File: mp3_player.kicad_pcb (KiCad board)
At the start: 4 copper layers, 0 parts

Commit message: PCB: outline, port cutouts, ESP32 placement
- board outline from pcb_outline_B.dxf, centred on the page, drill/place
  and grid origin at the bottom-left corner (130, 155)
- USB-C and jack cutouts drawn on the board outline instead of the
  footprints; jack pads trimmed for 0.2 mm to the slot, custom DRC rule
  allows 0.2 mm edge clearance for those pads only
- ESP32 on the centre line with the antenna at the top edge, antenna
  keepout on all copper layers
- microSD peg holes made non-plated

Co-Authored-By: Claude Opus 5.5 <noreply@anthropic.com>
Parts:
- added BT1: Battery_Cell, mp3_player:CONN-SMD_2P-P1.00_SM02B-SRSS-TB-LF-SN, F.Cu at (210.1, 74.1)
- added C1: C, Capacitor_SMD:C_0402_1005Metric, F.Cu at (208.7, 62.0)
- added C10: C, Capacitor_SMD:C_0603_1608Metric, F.Cu at (207.7, 100.3)
- added C11: C, Capacitor_SMD:C_0402_1005Metric, F.Cu at (208.7, 69.9)
- added C12: C, Capacitor_SMD:C_0603_1608Metric, F.Cu at (207.7, 102.9)
- added C13: C, Capacitor_SMD:C_0603_1608Metric, F.Cu at (211.7, 92.8)
- added C14: C, Capacitor_SMD:C_0603_1608Metric, F.Cu at (211.7, 95.3)
- added C15: C, Capacitor_SMD:C_0603_1608Metric, F.Cu at (211.7, 97.8)
- added C16: C, Capacitor_SMD:C_0402_1005Metric, F.Cu at (211.5, 62.0)
- added C17: C, Capacitor_SMD:C_0805_2012Metric, F.Cu at (225.4, 85.2)
- added C18: C, Capacitor_SMD:C_0402_1005Metric, F.Cu at (211.5, 64.0)
- added C19: C, Capacitor_SMD:C_0603_1608Metric, F.Cu at (211.7, 100.3)
- added C2: C, Capacitor_SMD:C_0603_1608Metric, F.Cu at (207.7, 92.8)
- added C20: C, Capacitor_SMD:C_0402_1005Metric, F.Cu at (211.5, 65.9)
- added C21: C, Capacitor_SMD:C_0603_1608Metric, F.Cu at (211.7, 102.9)
- added C22: C, Capacitor_SMD:C_0402_1005Metric, F.Cu at (211.5, 67.9)
- added C23: C, Capacitor_SMD:C_0805_2012Metric, F.Cu at (225.4, 88.2)
- added C24: C, Capacitor_SMD:C_0402_1005Metric, F.Cu at (211.5, 69.9)
- added C25: C, Capacitor_SMD:C_0402_1005Metric, F.Cu at (214.4, 62.0)
- added C26: C, Capacitor_SMD:C_0402_1005Metric, F.Cu at (214.4, 64.0)
- added C27: C, Capacitor_SMD:C_0603_1608Metric, F.Cu at (215.7, 92.8)
- added C28: C, Capacitor_SMD:C_0402_1005Metric, F.Cu at (214.4, 65.9)
- added C29: C, Capacitor_SMD:C_0603_1608Metric, F.Cu at (215.7, 95.3)
- added C3: C, Capacitor_SMD:C_0402_1005Metric, F.Cu at (208.7, 64.0)
- added C30: C, Capacitor_SMD:C_0402_1005Metric, F.Cu at (214.4, 67.9)
- added C31: C, Capacitor_SMD:C_0603_1608Metric, F.Cu at (215.7, 97.8)
- added C32: C, Capacitor_SMD:C_0603_1608Metric, F.Cu at (215.7, 100.3)
- added C33: C, Capacitor_SMD:C_0402_1005Metric, F.Cu at (214.4, 69.9)
- added C34: C, Capacitor_SMD:C_0603_1608Metric, F.Cu at (215.7, 102.9)
- added C35: C, Capacitor_SMD:C_0402_1005Metric, F.Cu at (217.3, 62.0)
- added C36: C, Capacitor_SMD:C_0603_1608Metric, F.Cu at (219.7, 92.8)
- added C37: C, Capacitor_SMD:C_0402_1005Metric, F.Cu at (217.3, 64.0)
- added C38: C, Capacitor_SMD:C_0603_1608Metric, F.Cu at (219.7, 95.3)
- added C39: C, Capacitor_SMD:C_0603_1608Metric, F.Cu at (219.7, 97.8)
- added C4: C, Capacitor_SMD:C_0805_2012Metric, F.Cu at (225.4, 79.1)
- added C40: C, Capacitor_SMD:C_0402_1005Metric, F.Cu at (217.3, 65.9)
- added C41: C, Capacitor_SMD:C_0402_1005Metric, F.Cu at (217.3, 67.9)
- added C42: C, Capacitor_SMD:C_0603_1608Metric, F.Cu at (219.7, 100.3)
- added C43: C, Capacitor_SMD:C_0603_1608Metric, F.Cu at (219.7, 102.9)
- added C44: 100nF, Capacitor_SMD:C_0402_1005Metric, F.Cu at (217.3, 69.9)
- added C5: C, Capacitor_SMD:C_0603_1608Metric, F.Cu at (207.7, 95.3)
- added C6: C, Capacitor_SMD:C_0402_1005Metric, F.Cu at (208.7, 65.9)
- added C7: C, Capacitor_SMD:C_0402_1005Metric, F.Cu at (208.7, 67.9)
- added C8: C, Capacitor_SMD:C_0603_1608Metric, F.Cu at (207.7, 97.8)
- added C9: C, Capacitor_SMD:C_0805_2012Metric, F.Cu at (225.4, 82.1)
- added CN1: PJ-342C CB, mp3_player:AUDIO-SMD_HX-PJ-342C, F.Cu at (159.3, 147.9)
- added Card3: TF-01A, mp3_player:TF-SMD_TF-01A, F.Cu at (198.4, 67.4)
- added D1: USBLC6-2SC6, mp3_player:SOT-23-6_L2.9-W1.6-P0.95-LS2.8-BL, F.Cu at (183.0, 96.3)
- added D2: D_Schottky, Diode_SMD:D_SOD-123, F.Cu at (222.0, 110.7)
- added FPC4: FH12-10S-0.5SH, mp3_player:FPC-SMD_FH12-10S-0.5SH-55, F.Cu at (224.2, 72.0)
- added L1: WPN201610HR47MT, mp3_player:IND-SMD_L2.0-W1.6_WPN2016X, F.Cu at (186.7, 104.1)
- added Q1: MMBT3904-C20526, mp3_player:SOT-23-3_L2.9-W1.3-P1.90-LS2.4-BR, F.Cu at (191.5, 108.5)
- added Q2: MMBT3904-C20526, mp3_player:SOT-23-3_L2.9-W1.3-P1.90-LS2.4-BR, F.Cu at (195.5, 108.5)
- added R1: R, Resistor_SMD:R_0402_1005Metric, F.Cu at (207.2, 78.6)
- added R10: R, Resistor_SMD:R_0402_1005Metric, F.Cu at (210.1, 82.6)
- added R11: R, Resistor_SMD:R_0402_1005Metric, F.Cu at (210.1, 84.6)
- added R12: R, Resistor_SMD:R_0402_1005Metric, F.Cu at (210.1, 86.6)
- added R13: R, Resistor_SMD:R_0402_1005Metric, F.Cu at (210.1, 88.6)
- added R14: R, Resistor_SMD:R_0402_1005Metric, F.Cu at (210.1, 90.6)
- added R15: R, Resistor_SMD:R_0402_1005Metric, F.Cu at (213.0, 78.6)
- added R16: R, Resistor_SMD:R_0402_1005Metric, F.Cu at (213.0, 80.6)
- added R17: R, Resistor_SMD:R_0402_1005Metric, F.Cu at (213.0, 82.6)
- added R18: R, Resistor_SMD:R_0402_1005Metric, F.Cu at (213.0, 84.6)
- added R19: R, Resistor_SMD:R_0402_1005Metric, F.Cu at (213.0, 86.6)
- added R2: R, Resistor_SMD:R_0402_1005Metric, F.Cu at (207.2, 80.6)
- added R20: R, Resistor_SMD:R_0402_1005Metric, F.Cu at (213.0, 88.6)
- added R21: R, Resistor_SMD:R_0402_1005Metric, F.Cu at (213.0, 90.6)
- added R22: R, Resistor_SMD:R_0402_1005Metric, F.Cu at (215.9, 78.6)
- added R23: R, Resistor_SMD:R_0402_1005Metric, F.Cu at (215.9, 80.6)
- added R24: R, Resistor_SMD:R_0402_1005Metric, F.Cu at (215.9, 82.6)
- added R25: R, Resistor_SMD:R_0402_1005Metric, F.Cu at (215.9, 84.6)
- added R26: R, Resistor_SMD:R_0402_1005Metric, F.Cu at (215.9, 86.6)
- added R27: R, Resistor_SMD:R_0402_1005Metric, F.Cu at (215.9, 88.6)
- added R28: R, Resistor_SMD:R_0402_1005Metric, F.Cu at (215.9, 90.6)
- added R29: R, Resistor_SMD:R_0402_1005Metric, F.Cu at (218.8, 78.6)
- added R3: R, Resistor_SMD:R_0402_1005Metric, F.Cu at (207.2, 82.6)
- added R30: R, Resistor_SMD:R_0402_1005Metric, F.Cu at (218.8, 80.6)
- added R31: R, Resistor_SMD:R_0402_1005Metric, F.Cu at (218.8, 82.6)
- added R32: R, Resistor_SMD:R_0402_1005Metric, F.Cu at (218.8, 84.6)
- added R33: R, Resistor_SMD:R_0402_1005Metric, F.Cu at (218.8, 86.6)
- added R34: R, Resistor_SMD:R_0402_1005Metric, F.Cu at (218.8, 88.6)
- added R35: R, Resistor_SMD:R_0402_1005Metric, F.Cu at (218.8, 90.6)
- added R36: R, Resistor_SMD:R_0402_1005Metric, F.Cu at (221.7, 78.6)
- added R37: R, Resistor_SMD:R_0402_1005Metric, F.Cu at (221.7, 80.6)
- added R38: R, Resistor_SMD:R_0402_1005Metric, F.Cu at (221.7, 82.6)
- added R39: R, Resistor_SMD:R_0402_1005Metric, F.Cu at (221.7, 84.6)
- added R4: R, Resistor_SMD:R_0402_1005Metric, F.Cu at (207.2, 84.6)
- added R40: R, Resistor_SMD:R_0402_1005Metric, F.Cu at (221.7, 86.6)
- added R41: R, Resistor_SMD:R_0402_1005Metric, F.Cu at (221.7, 88.6)
- added R42: R, Resistor_SMD:R_0402_1005Metric, F.Cu at (221.7, 90.6)
- added R5: R, Resistor_SMD:R_0402_1005Metric, F.Cu at (207.2, 86.6)
- added R6: R, Resistor_SMD:R_0402_1005Metric, F.Cu at (207.2, 88.6)
- added R7: R, Resistor_SMD:R_0402_1005Metric, F.Cu at (207.2, 90.6)
- added R8: R, Resistor_SMD:R_0402_1005Metric, F.Cu at (210.1, 78.6)
- added R9: R, Resistor_SMD:R_0402_1005Metric, F.Cu at (210.1, 80.6)
- added SW1: TS-1088-AR02016, mp3_player:SW-SMD_L3.9-W3.0-P4.45, F.Cu at (225.0, 93.7)
- added SW2: EVQP7J01P, mp3_player:SW-SMD_EVQP7J01P, F.Cu at (222.2, 106.2)
- added SW3: TS-1088-AR02016, mp3_player:SW-SMD_L3.9-W3.0-P4.45, F.Cu at (225.0, 97.9)
- added SW4: TS-1187B-B, mp3_player:KEY-SMD_4P-L4.8-W4.8-P3.70-LS6.4-TL, F.Cu at (185.0, 64.6)
- added SW5: TS-1187B-B, mp3_player:KEY-SMD_4P-L4.8-W4.8-P3.70-LS6.4-TL, F.Cu at (185.0, 71.2)
- added SW6: TS-1187B-B, mp3_player:KEY-SMD_4P-L4.8-W4.8-P3.70-LS6.4-TL, F.Cu at (185.0, 77.8)
- added SW7: TS-1187B-B, mp3_player:KEY-SMD_4P-L4.8-W4.8-P3.70-LS6.4-TL, F.Cu at (185.0, 84.5)
- added SW8: TS-1187B-B, mp3_player:KEY-SMD_4P-L4.8-W4.8-P3.70-LS6.4-TL, F.Cu at (185.0, 91.1)
- added U1: CP2102N-A02-GQFN24R, mp3_player:QFN-24_L4.0-W4.0-P0.50-TL-EP2.6, F.Cu at (200.8, 109.3)
- added U2: BQ25180YBGR, mp3_player:DSBGA-8_L1.6-W0.9-R2-C4-P0.40-BL, F.Cu at (186.7, 99.6)
- added U3: LM27762DSSR, mp3_player:WSON-12_L3.0-W2.0-P0.50-BL-EP, F.Cu at (182.9, 104.6)
- added U4: TPS63802DLAR, mp3_player:VSON-10_L3.0-W2.0-P0.50-TL, F.Cu at (182.5, 109.0)
- added U5: MAX17048G+T10, mp3_player:TDFN-8_L2.0-W2.0-P0.50-BL-EP1.2, F.Cu at (186.0, 108.5)
- added U6: LP5907MFX-3.3/NOPB, mp3_player:SOT-23-5_L3.0-W1.7-P0.95-LS2.8-BR, F.Cu at (182.8, 100.6)
- added U7: ESP32-PICO-MINI-02-N8R2, mp3_player:BULETM-SMD_ESP32-PICO-MINI-02-N8R2, F.Cu at (149.1, 66.5)
- added U8: OPA1622IDRCR, mp3_player:VSON-10_L3.0-W3.0-P0.50-BL-EP1.65, F.Cu at (215.4, 73.2)
- added U9: PCM5122PW, mp3_player:TSSOP-28_L9.8-W6.6-P0.65-BL, F.Cu at (224.3, 65.1)
- added USB1: TYPE-C 16P CB0.8 073, mp3_player:USB-C-SMD_TYPE-C-16P-CB0.8-073, F.Cu at (138.9, 150.3)
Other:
- board outline added: 38.2 x 99.6 mm

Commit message: PCB: tall parts on the back, top strip layout, centred power key
- USB-C, jack, ESP32, microSD and power switch on the back of the board,
  as the enclosure B model assumes (front stack is only 1.6 mm)
- top strip: microSD left (stays inside, no shell slot), ESP32 right with
  the antenna at the top edge, power switch at the right edge
- power switch hangs under the PCB, so its actuator lands 0.1 mm from
  mid-thickness; the side opening is now centred on the shell
- antenna keepout narrowed to the antenna side of the top strip
- concept.py follows the new positions; the ESP32 no longer hits the cap
  and the SD socket no longer hits the battery

Co-Authored-By: Claude Opus 5.5 <noreply@anthropic.com>
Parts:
- CN1, Card3, SW2, U7, USB1: moved to B.Cu
- moved SW2 67.1 mm to (166.6, 68.6), turned to -90 degrees
- moved Card3 58.5 mm to (139.9, 65.5), turned to 90 degrees
- moved U7 8.50 mm to (157.6, 66.5), turned to 180 degrees
- turned USB1 to 180 degrees

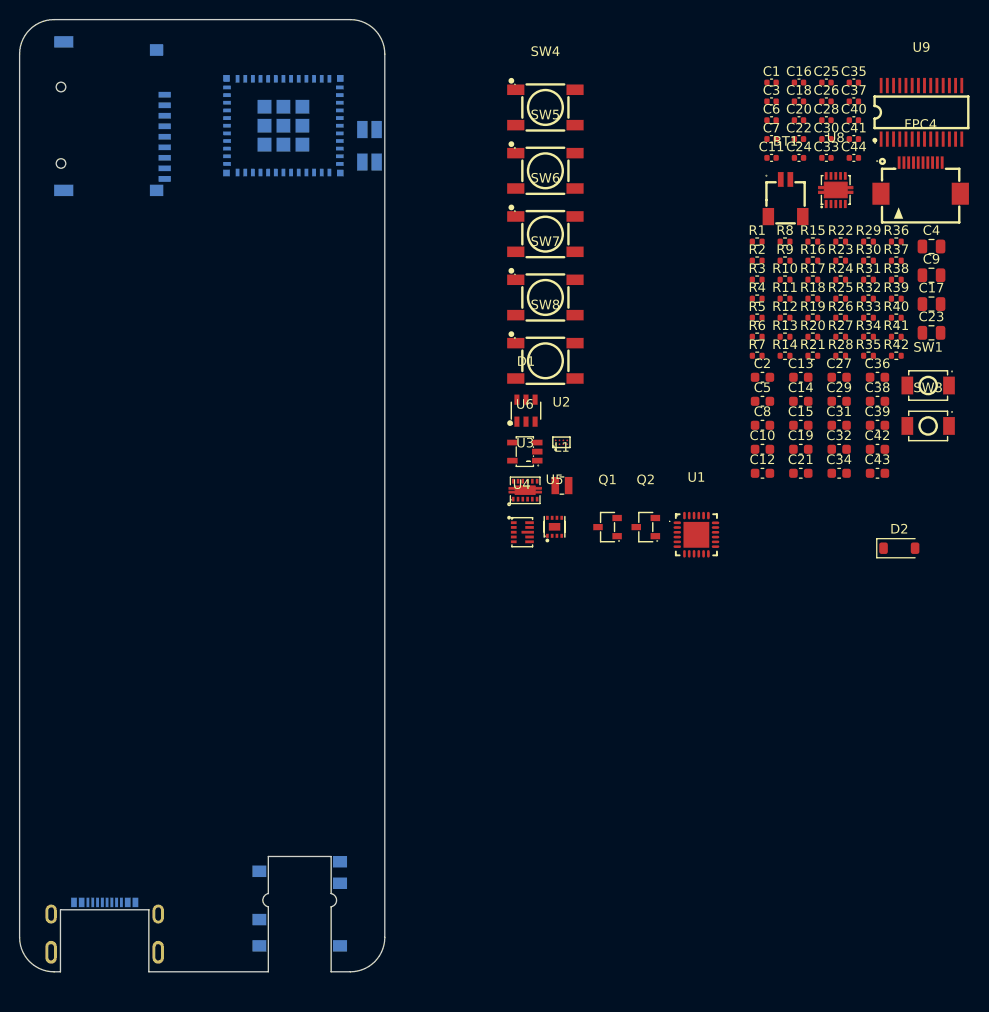
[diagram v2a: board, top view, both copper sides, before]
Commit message: PCB: place the remaining chips and the buttons
- power corner on the back, bottom-left between the battery end and
  USB-C: battery connector, BQ25180, MAX17048, USBLC6, TPS63802 + L1
- CP2102N with the auto-reset transistors on the front, bottom-left
- PCM5122 + LP5907 in the middle band, ~40 mm from the inductor;
  OPA1622 at the jack on the front, LM27762 behind it on the back
- click wheel switches on the ring, EN/BOOT on the back under the ramp
- space under the display kept free for a low-profile FPC connector
  (FH12 is too tall for either side)

Co-Authored-By: Claude Opus 5.5 <noreply@anthropic.com>
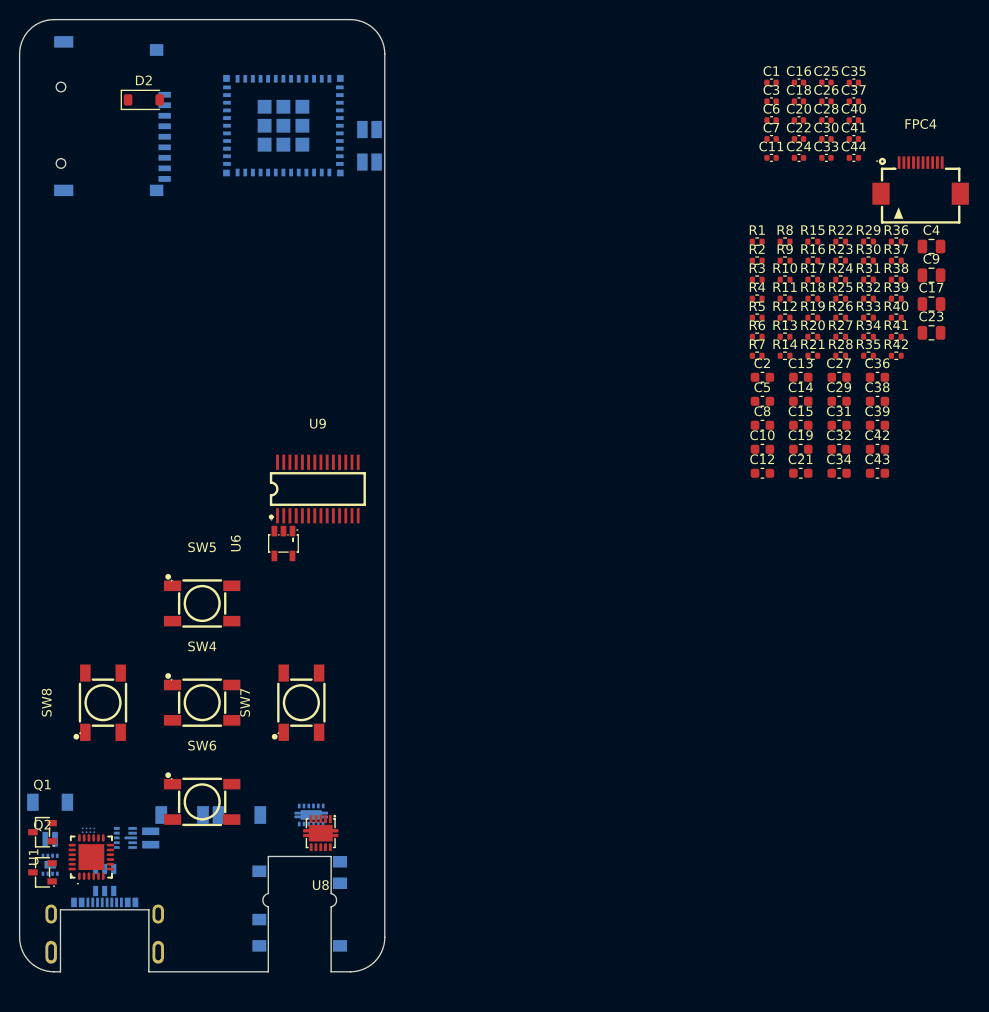
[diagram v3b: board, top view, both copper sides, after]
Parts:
- BT1, D1, L1, SW1, SW3, U2, U3, U4, U5: moved to B.Cu
- moved BT1 100.8 mm to (133.2, 139.2)
- moved D2 91.9 mm to (143.0, 63.8)
- moved SW1 90.0 mm to (147.0, 138.6)
- moved U8 86.2 mm to (161.5, 140.5), turned to 180 degrees
- moved SW3 82.7 mm to (153.0, 138.6)
- moved U9 74.4 mm to (161.2, 104.5)
- moved Q2 72.7 mm to (132.4, 144.6)
- moved SW4 71.9 mm to (149.1, 126.8)
- moved U1 71.7 mm to (137.5, 143.0), turned to 90 degrees
- moved SW6 69.4 mm to (149.1, 137.2)
- moved Q1 67.2 mm to (132.4, 140.4)
- moved D1 66.0 mm to (138.9, 145.4)
- moved U2 64.0 mm to (137.2, 140.2)
- moved U5 63.5 mm to (133.2, 143.8)
- moved SW8 58.5 mm to (138.7, 126.8), turned to 90 degrees
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
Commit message: Display connector: FH19C-10S, placed under the display
- FH12 (2.0 mm) fits neither side of the board; FH19C-10S-0.5SH(10)
  (C598004) is 0.9 mm tall, bottom contact, same 10 pins
- footprint and 3D model from LCSC added to the project library;
  schematic fields (value, footprint, datasheet, LCSC) updated
- FPC4 on the front at (149.1, 110.1), opening toward the display: the
  LCD tail lies flat into it, flex pin 1 and connector pin 1 both on
  the right
- docs: BOM, placement checklist and connections.md follow the swap

Co-Authored-By: Claude Opus 5.5 <noreply@anthropic.com>
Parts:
- FPC4: value FH12-10S-0.5SH -> FH19C-10S-0.5SH(10); footprint mp3_player:FPC-SMD_FH12-10S-0.5SH-55 -> mp3_player:FPC-SMD_10P-P0.50_FH19C-10S-0.5SH-10
- moved FPC4 84.3 mm to (149.1, 110.1), turned to 180 degrees

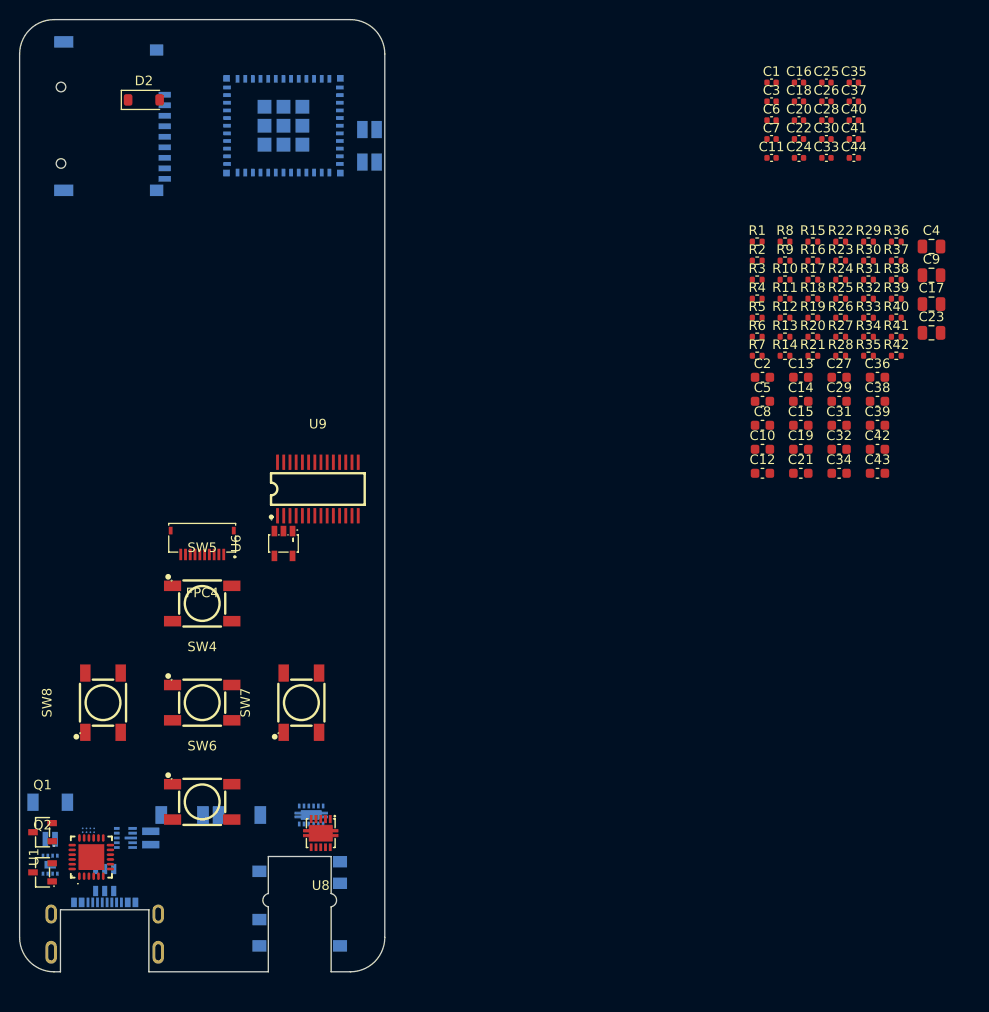
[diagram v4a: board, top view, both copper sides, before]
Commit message: PCB: place all resistors and capacitors
- every passive sits next to the pin it serves, rotated so its non-GND
  pad faces that pin; decoupling caps hug their supply pins
- back: power corner (BQ25180, TPS63802, MAX17048, USB-C CC/VBUS),
  LM27762 pump, feedback and output caps, jack detect and bleeders,
  ESP32 3V3 and microSD decoupling, SD_CLK series resistor at the source
- front: CP2102N, PCM5122, LP5907, OPA1622 (supply caps, RC input
  filter, EN divider), display caps, pull-ups grouped by ESP32 pin side
- U6 LP5907 moved to (165.2, 113.2) to free the DAC charge-pump pins;
  U8 OPA1622 moved up 0.6 mm so its EN trace clears the jack cutout
- all parts checked against the enclosure: nothing under the battery,
  ramp height respected, nothing under the display, no 0603/0805 under
  the wheel ring. DRC: 0 errors, silkscreen warnings left for cleanup

Co-Authored-By: Claude Opus 5.5 <noreply@anthropic.com>
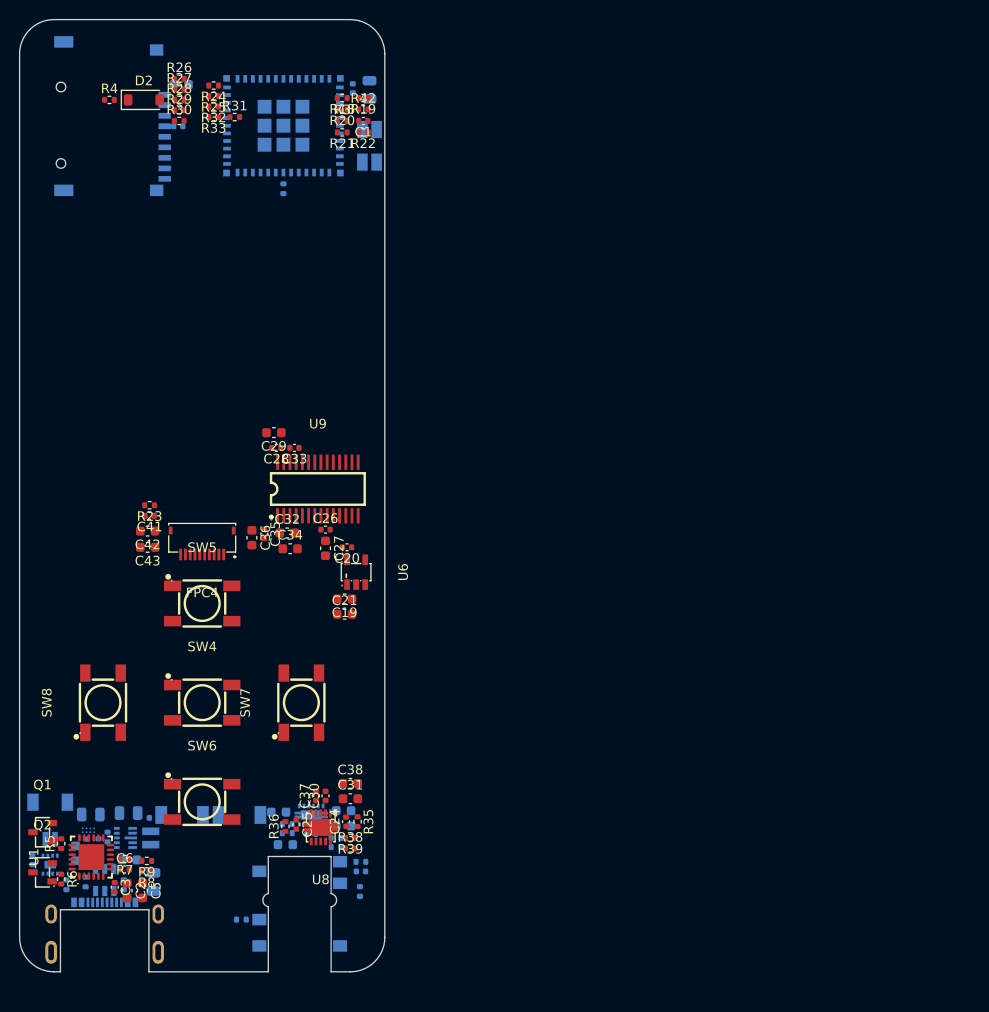
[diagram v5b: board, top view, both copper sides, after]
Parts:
- C10, C11, C12, C13, C14, C15, C16, C17, C18, C22, C23, C39, C4, C40, C44, C7, C8, C9, R1, R10, R11, R12, R13, R14, R15, R16, R17, R2, R34, R37, R40, R41: moved to B.Cu
- moved C18 112.8 mm to (131.3, 143.3), turned to -90 degrees
- moved C3 107.1 mm to (139.9, 146.2), turned to -90 degrees
- moved C4 105.1 mm to (144.0, 145.6), turned to 90 degrees
- moved C9 104.5 mm to (137.4, 138.6)
- moved C6 103.5 mm to (141.0, 144.3)
- moved C7 102.8 mm to (137.1, 141.6), turned to -90 degrees
- moved C16 102.3 mm to (144.1, 138.9)
- moved R17 100.5 mm to (134.9, 145.9), turned to -90 degrees
- moved C17 99.4 mm to (141.4, 138.4), turned to 180 degrees
- moved R15 97.7 mm to (138.2, 141.6), turned to -90 degrees
- moved R1 97.1 mm to (136.9, 145.6), turned to 90 degrees
- moved C25 95.4 mm to (158.9, 139.6), turned to -90 degrees
- moved R16 95.3 mm to (139.2, 140.9), turned to -90 degrees
- moved R8 93.8 mm to (143.3, 144.5), turned to 180 degrees
- moved R2 93.0 mm to (140.9, 145.9), turned to 90 degrees
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
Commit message: PCB: GND plane on In1, first routing (CP2102N decoupling)
- GND zone on the inner GND layer, whole board
- C2, C3, C5, C6 routed to U1 pins 6/7 with 0.25 mm tracks
- C2/C3/C5 share one GND via (kept off the USB-C GND pad on the back),
  C6 has its own GND via

Co-Authored-By: Claude Opus 5.5 <noreply@anthropic.com>
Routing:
- net +3V3: track 0.00 -> 5.44 mm
- net GND: track 0.00 -> 4.51 mm, vias 0 -> 2
- added copper zone on In1.Cu, net GND
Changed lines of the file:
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@@
 		(layer "Edge.Cuts")
+	)
+	(segment
+		(start 140.005 145.725)
+		(end 139.95 145.67)
+		(width 0.25)
+		(layer "F.Cu")
+		(net "+3V3")
+	)
+	(segment
+		(start 140.52 144.3)
+		(end 139.55 144.3)
+		(width 0.25)
+		(layer "F.Cu")
+		(net "+3V3")
+	)
+	(segment
+		(start 139.95 145.67)
+		(end 139.42 145.67)
+		(width 0.25)
+		(layer "F.Cu")
+		(net "+3V3")
+	)
+	(segment
+		(start 141.25 145.725)
+		(end 140.005 145.725)
+		(width 0.25)
+		(layer "F.Cu")
+		(net "+3V3")
+	)
+	(segment
+		(start 139.55 144.3)
+		(end 139.5 144.25)
+		(width 0.25)
+		(layer "F.Cu")
+		(net "+3V3")
+	)
+	(segment
+		(start 139.42 145.67)
+		(end 138.75 145)
+		(width 0.25)
+		(layer "F.Cu")
+		(net "+3V3")
+	)
+	(segment
+		(start 142.85 145.725)
+		(end 141.25 145.725)
+		(width 0.25)
+		(layer "F.Cu")
+		(net "+3V3")
+	)
+	(segment
+		(start 140.595 147.275)
+		(end 139.95 146.63)
+		(width 0.25)
+		(layer "F.Cu")
+		(net "GND")
+	)
+	(segment
+		(start 142.85 147.275)
+		(end 142 147.275)
+		(width 0.25)
+		(layer "F.Cu")
+		(net "GND")
+	)
+	(segment
+		(start 142 147.275)
+		(end 141.25 147.275)
+		(width 0.25)
+		(layer "F.Cu")
+		(net "GND")
+	)
+	(segment
+		(start 141.25 147.275)
+		(end 140.595 147.275)
+		(width 0.25)
+		(layer "F.Cu")
+		(net "GND")
+	)
+	(segment
+		(start 142 147.275)
+		(end 142.11 147.165)
+		(width 0.25)
+		(layer "F.Cu")
+		(net "GND")
+	)
+	(segment
+		(start 142.11 147.165)
+		(end 142.11 146.5)
+		(width 0.25)
+		(layer "F.Cu")
+		(net "GND")
+	)
+	(segment
+		(start 141.48 144.3)
+		(end 141.894176 144.3)
+		(width 0.25)
+		(layer "F.Cu")
+		(net "GND")
+	)
+	(segment
+		(start 141.894176 144.3)
+		(end 141.972581 144.221595)
+		(width 0.25)
+		(layer "F.Cu")
+		(net "GND")
+	)
+	(via
+		(at 141.972581 144.221595)
+		(size 0.6)
+		(drill 0.3)
+		(layers "F.Cu" "B.Cu")
+		(net "GND")
+	)
+	(via
+		(at 142.11 146.5)
+		(size 0.6)
+		(drill 0.3)
+		(layers "F.Cu" "B.Cu")
+		(net "GND")
 	)
 	(zone
@@
 			)
 		)
+	)
+	(zone
+		(net "GND")
+		(layer "In1.Cu")
+		(name "GND")
+		(hatch edge 0.5)
+		(connect_pads
+			(clearance 0.5)
+		)
+		(min_thickness 0.25)
+		(fill yes
+			(thermal_gap 0.5)
+			(thermal_bridge_width 0.5)
+			(island_removal_mode 0)
+		)
+		(polygon
+			(pts
+				(xy 130 55.5) (xy 168.2 55.5) (xy 168.2 155) (xy 130.5 155) (xy 130 154.5)
+			)
+		)
